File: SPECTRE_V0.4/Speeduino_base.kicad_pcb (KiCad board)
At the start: 2 copper layers, 100 x 93 mm, 161 parts, among them IC1 LM340?-MP, J1 Conn_01x04_Male, Q1 2N7002, Q10 BSP78, Q11 BSP78, Q12 BSP78, Q13 BSP78, Q2 CJ2302, Q3 CJ2302, Q4 CJ2302, Q5 BSP78, Q6 BSP78, Q7 CJ2302, Q8 CJ2302, Q9 CJ2302, U1 MAX9926UAEE+, U2 molex_48pin

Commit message: Cleaned up V0.4 Bug fixes in board V0.4 Changed readme to add more to be tested functions
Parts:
- added D22: D_Small, Diode_SMD:D_SOD-128, F.Cu at (85.3, 11.4)
- added D23: D_Small, Diode_SMD:D_SOD-128, F.Cu at (85.3, 15.5)
- added D24: D_Small, Diode_SMD:D_SOD-128, F.Cu at (92.7, 11.4)
- added D25: D_Small, Diode_SMD:D_SOD-128, F.Cu at (92.7, 15.5)
- added R73: 1k, Speeduino_base:R0603, F.Cu at (149.9, 15.9)
- added R74: 1k, Speeduino_base:R0603, F.Cu at (152.3, 15.9)
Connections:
- C15 pad 2: /PC6 -> /PC5
- D12 pad 3: /PC6 -> /PC5
- JP11 pad 2: Net-(D1-Pad3) -> Net-(JP11-Pad2)
- JP12 pad 2: Net-(D4-Pad3) -> Net-(JP12-Pad2)
- R27 pad 1: /PA6 -> /PA4
- R28 pad 2: Net-(R28-Pad2) -> 3.3V
- R33 pad 2: /PC6 -> /PC5

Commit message: Lots of changes, started new PCB with 8 inj channels.
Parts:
- removed F3, F4: PPTC 16V2A, Speeduino_base:1812L
- removed F5, F6, F7: PPTC 16V2A, Fuse:Fuse_1812_4532Metric
- removed IC1: LM340?-MP, Speeduino_base:SOT223
- removed JP15, JP5, JP6, JP7, JP8: SolderJumper_3_Bridged12, Jumper:SolderJumper-3_P1.3mm_Bridged12_Pad1.0x1.5mm
- removed U$1: A4988BREAKOUT, Speeduino_base:A4988BREAKOUT
- added A1: Pololu_Breakout_DRV8825, Module:Pololu_Breakout-16_15.2x20.3mm, F.Cu at (183.0, 65.8)
- added D26: 1N4007, Diode_SMD:D_SOD-128, B.Cu at (207.6, 43.8)
- added F2: PPTC 16V2A, Resistor_SMD:R_1812_4532Metric_Pad1.30x3.40mm_HandSolder, F.Cu at (176.7, 48.5)
- added Q14: BSP78, Speeduino_base:SOT223, F.Cu at (177.2, 89.9)
- added Q15: BSP78, Speeduino_base:SOT223, B.Cu at (191.0, 60.2)
- added Q16: BSP78, Speeduino_base:SOT223, B.Cu at (191.0, 42.6)
- added Q17: BSP78, Speeduino_base:SOT223, B.Cu at (191.0, 51.4)
- added Q18: BSP78, Speeduino_base:SOT223, B.Cu at (191.0, 33.8)
- added R75: 10k, Resistor_SMD:R_0603_1608Metric_Pad1.05x0.95mm_HandSolder, F.Cu at (145.7, 102.1)
- added R76: 10k, Resistor_SMD:R_0603_1608Metric_Pad1.05x0.95mm_HandSolder, F.Cu at (145.7, 106.7)
- added R77: 100, Speeduino_base:R0603, F.Cu at (164.6, 89.9)
- added R78: 10k, Speeduino_base:R0603, F.Cu at (168.3, 89.9)
- added R79: 10k, Speeduino_base:R0603, F.Cu at (170.7, 37.5)
- added R80: 10k, Speeduino_base:R0603, F.Cu at (174.5, 37.5)
- added R81: 10k, Speeduino_base:R0603, F.Cu at (168.8, 37.5)
- added R82: 10k, Speeduino_base:R0603, F.Cu at (172.6, 37.5)
- added U3: LM78M05_TO220, Package_TO_SOT_THT:TO-220-3_Vertical, F.Cu at (132.0, 37.8)
- D22, D23, D24, D25: value D_Small -> 1N4007
- F1: footprint Speeduino_base:1812L -> Resistor_SMD:R_1812_4532Metric_Pad1.30x3.40mm_HandSolder
- J1: footprint Connector_PinHeader_2.54mm:PinHeader_1x04_P2.54mm_Vertical -> Connector_PinHeader_2.00mm:PinHeader_1x04_P2.00mm_Vertical_SMD_Pin1Left
- R2: footprint Speeduino_base:R0603 -> Resistor_SMD:R_0603_1608Metric_Pad1.05x0.95mm_HandSolder
- R23: footprint Speeduino_base:R-7,5 -> Varistor:RV_Disc_D12mm_W3.9mm_P7.5mm
- moved D22 94.0 mm to (167.0, 58.0), turned to 90 degrees
- moved D25 93.2 mm to (182.8, 39.3), turned to 270 degrees
- moved D24 90.2 mm to (178.4, 39.4), turned to 270 degrees
- moved D23 88.4 mm to (162.8, 58.1), turned to 90 degrees
- moved C15 83.3 mm to (166.5, 22.1), turned to 180 degrees
- moved C12 81.4 mm to (169.1, 22.1), turned to 180 degrees
- moved R33 81.2 mm to (174.3, 22.1)
- moved R31 80.7 mm to (171.7, 22.1), turned to 180 degrees
- moved R30 80.6 mm to (176.9, 22.1), turned to 0 degrees
- moved D12 79.9 mm to (162.5, 23.7)
- moved R54 66.2 mm to (203.8, 99.4), turned to 180 degrees
- moved D9 64.0 mm to (201.9, 102.4), turned to 270 degrees
- moved R26 63.6 mm to (201.9, 99.4), turned to 180 degrees
- moved D17 62.1 mm to (203.8, 102.4), turned to 270 degrees
- moved R74 60.3 mm to (121.2, 67.6), turned to 180 degrees
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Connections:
- net /PA0 renamed PA0
- net /PA11 renamed Net-(JP3-Pad32)
- net /PA12 renamed Net-(JP3-Pad31)
- net /PA15 renamed Net-(JP3-Pad30)
- net /PA5 renamed PA5
- net /PA6 renamed Net-(JP1-Pad29)
- net /PA7 renamed Net-(JP1-Pad30)
- net /PA8 renamed PA8
- net /PB0 renamed Net-(JP1-Pad33)
- net /PB11 renamed PB11
- net /PB12 renamed PB12
- net /PB13 renamed PB13
- net /PB14 renamed PB14
- net /PB15 renamed PB15
- net /PB3 renamed PB3
- net /PB5 renamed PB5
- net /PB6 renamed PB6
- net /PB7 renamed PB7
- net /PB8 renamed PB8
- net /PB9 renamed PB9
- net /PC0 renamed PC0
- net /PC10 renamed Net-(JP3-Pad29)
- net /PC11 renamed Net-(JP3-Pad28)
- net /PC12 renamed Net-(JP3-Pad27)
- net /PC2 renamed PC2
- net /PC4 renamed PC4
- net /PC5 renamed PC5
- net /PC6 renamed PC6
- net /PC9 renamed Net-(JP3-Pad36)
- net /PD0 renamed PD0
- net /PD1 renamed PD1
- net /PD11 renamed PD11
- net /PD2 renamed Net-(JP3-Pad24)
- net /PD4 renamed PD4
- net /PD5 renamed PD5
- net /PD6 renamed PD6
- net /PD7 renamed PD7
- net /PD8 renamed PD8
- net /PD9 renamed PD9
- net /PE10 renamed PE10
- net /PE15 renamed PE15
- net /PE4 renamed PE4
- net /PE6 renamed PE6
- net /PE8 renamed PE8
- net /PE9 renamed PE9
- net /VREF+ renamed Net-(JP1-Pad22)
- net /VREF- renamed Net-(JP1-Pad21)
- C13 pad 2: Net-(C13-Pad2) -> PC3
- C23 pad 2: Net-(C23-Pad2) -> PA1
- C24 pad 2: Net-(C24-Pad2) -> PC1
- D11 pad 3: /PC3 -> PC3
- D16 pad 3: /PC1 -> PC1
- D24 pad 2: IDLE2-OUT -> IDLE1-OUT
- D25 pad 2: IDLE1-OUT -> IDLE2-OUT
- JP1 pad 11: /PE2 -> PE2
- JP1 pad 12: /PE3 -> PE3
- JP1 pad 14: /PE5 -> PE5
- JP1 pad 18: /PC1 -> PC1
- JP1 pad 20: /PC3 -> PC3
- JP1 pad 27: /PA4 -> PA4
- JP1 pad 35: /PE7 -> PE7
- JP1 pad 39: /PE11 -> PE11
- JP1 pad 40: /PE12 -> PE12
- JP1 pad 41: /PE13 -> PE13
- JP1 pad 42: /PE14 -> PE14
- JP1 pad 44: /PB10 -> PB10
- JP10 pad 3: STEP_2A_OUT -> STEP_1A_OUT
- JP3 pad 38: /PC7 -> PC7
- JP3 pad 45: /PD10 -> PD10
- JP9 pad 3: STEP_1A_OUT -> STEP_2A_OUT
- Q10 pad 2: IDLE1-OUT -> IDLE2-OUT
- Q10 pad 4: IDLE1-OUT -> IDLE2-OUT
- Q11 pad 2: IDLE2-OUT -> IDLE1-OUT
- Q11 pad 4: IDLE2-OUT -> IDLE1-OUT
- Q3 pad 2: GND -> PWR_GND
- R14 pad 2: Net-(R14-Pad2) -> Net-(C6-Pad1)
- R26 pad 2: VBAT_F1 -> VBAT
- R27 pad 1: /PA4 -> PE3
- R32 pad 2: /PC3 -> PC3
- R39 pad 2: /PC1 -> PC1
- R44 pad 2: GND -> PWR_GND
- R54 pad 2: VBAT_F1 -> VBAT
- R6 pad 2: Net-(R6-Pad2) -> Net-(C5-Pad2)
- R65 pad 2: /PB10 -> PD10
- U1 pad 10: Net-(R14-Pad2) -> Net-(C6-Pad1)
- U1 pad 16: Net-(R6-Pad2) -> Net-(C5-Pad2)
- U2 pad 1: VBAT -> PWR_GND
- U2 pad 10: PWR_GND -> BARO
- U2 pad 11: Net-(JP8-Pad2) -> STEP_2B_OUT
- U2 pad 12: Net-(JP9-Pad2) -> STEP_1B_OUT
- U2 pad 13: STEP_2B_OUT -> IGN1-OUT
- U2 pad 15: FUEL_PUMP -> FAN
- U2 pad 16: INJ4-OUT -> IGN4-OUT
- U2 pad 17: Net-(JP10-Pad2) -> FUEL_PUMP
- U2 pad 18: VR2+ -> Net-(U2-Pad18)
- U2 pad 19: FAN -> VR2+
- U2 pad 2: VBAT -> PWR_GND
- U2 pad 20: INJ3-OUT -> Net-(JP9-Pad2)
- U2 pad 21: VR1- -> CLT_2
- U2 pad 23: TPS -> VR1-
- U2 pad 24: IGN1-OUT -> INJ4-OUT
- U2 pad 25: Net-(JP5-Pad2) -> GND
- U2 pad 28: INJ2-OUT -> INJ3-OUT
- U2 pad 29: Net-(JP6-Pad2) -> GND
- U2 pad 3: PWR_GND -> VBAT
- U2 pad 33: Net-(JP7-Pad2) -> GND
- U2 pad 34: 3.3V -> TPS
- U2 pad 37: V_O2 -> Net-(U2-Pad37)
- U2 pad 38: V_IGN -> FLEX_FUEL_IN
- U2 pad 4: PWR_GND -> VBAT
- U2 pad 41: V_IGN -> O2_2
- U2 pad 42: V_IGN -> IAT_2
- U2 pad 43: 5V -> Net-(U2-Pad43)
- U2 pad 44: IGN4-OUT -> INJ2-OUT
- U2 pad 45: V_IGN -> 5V
- U2 pad 46: PWR_GND -> 3.3V
- U2 pad 47: Net-(JP15-Pad2) -> BOOST-OUT
- U2 pad 5: V_INJ34 -> INJ8-OUT
- U2 pad 6: V_INJ34 -> INJ7-OUT
- U2 pad 7: V_INJ12 -> INJ5-OUT
- U2 pad 8: V_INJ12 -> INJ6-OUT
- U2 pad 9: PWR_GND -> Net-(JP10-Pad2)
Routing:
- net GND: track 625.1 -> 299.6 mm, vias 32 -> 4
- net 3.3V: track 559.6 -> 426.3 mm, vias 21 -> 8
- net PD13: track 143.4 -> 32.2 mm, vias 2 -> 0
- net VR2+: track 187.0 -> 77.0 mm, vias 2 -> 3
- net /PE5: track 105.6 -> 0.00 mm, vias 1 -> 0
- net Net-(Q4-Pad1): track 100.9 -> 5.86 mm, vias 4 -> 0
- net VR1-: track 176.3 -> 84.3 mm, vias 0 -> 3
- net VR2-: track 161.8 -> 74.1 mm, vias 0 -> 2
- net VR1+: track 195.1 -> 110.7 mm, vias 0 -> 3
- net BOOST-OUT: track 0.00 -> 82.6 mm, vias 0 -> 1
- net /PB10: track 81.6 -> 0.00 mm, vias 1 -> 0
- net Net-(JP15-Pad2): track 74.4 -> 0.00 mm, vias 1 -> 0
- net FLEX_FUEL_IN: track 6.26 -> 80.5 mm, vias 0 -> 1
- net PC13: track 69.6 -> 0.00 mm, vias 2 -> 0
- net VBAT_F1: track 100.7 -> 31.9 mm, vias 4 -> 0
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- removed copper zone on F.Cu, net 3.3V
- removed copper zone on F.Cu, net 5V
- removed copper zone on F.Cu, net IDLE1-OUT
- removed copper zone on F.Cu, net IDLE2-OUT
- removed copper zone on B.Cu, net INJ1-OUT
- removed copper zone on B.Cu, net INJ2-OUT
- removed copper zone on B.Cu, net INJ3-OUT
- removed copper zone on B.Cu, net INJ4-OUT
- removed copper zone on B.Cu, net PWR_GND
- removed copper zone on F.Cu, net VBAT
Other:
- board text added: "SPEEDUINO STM32F4 TESTBOARD NR4"
- board text removed: "SPEEDUINO STM32F4 TESTBOARD NR3"

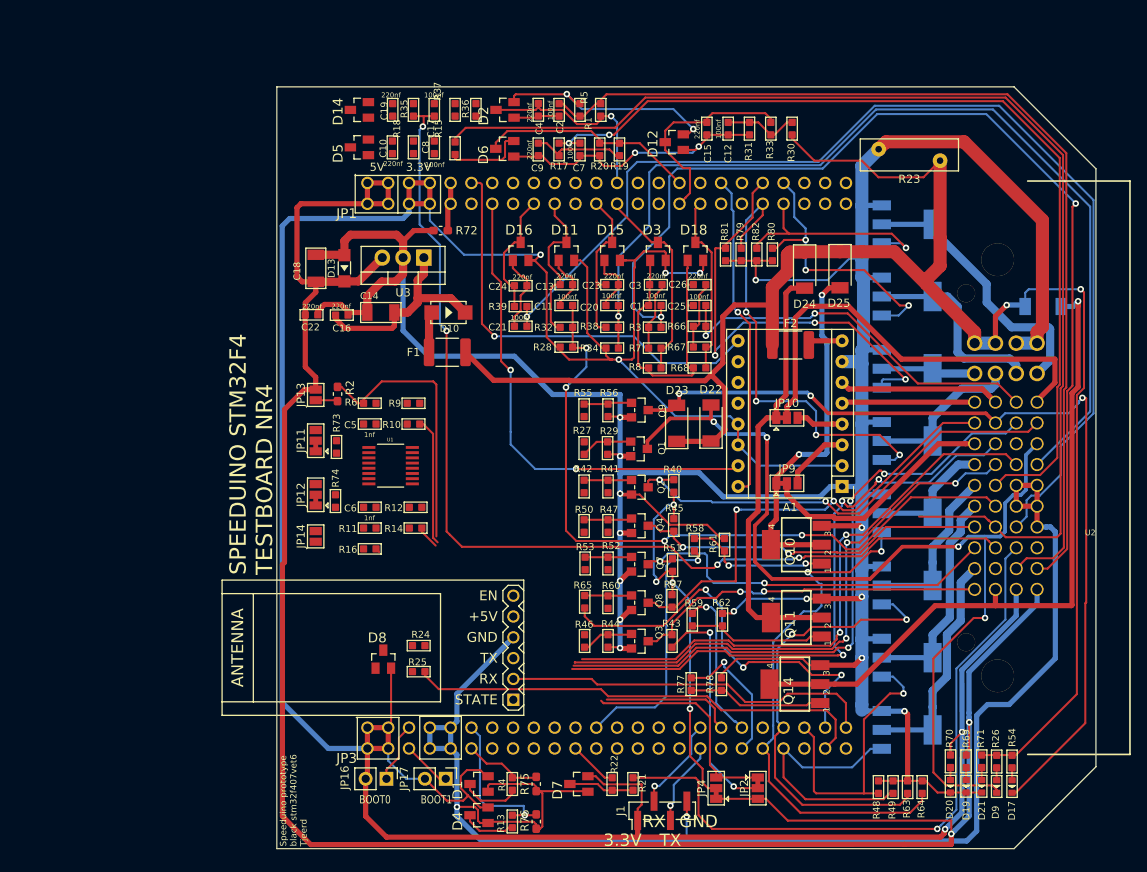
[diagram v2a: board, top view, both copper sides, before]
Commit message: All tracks routed: TODO: Copper GND, Copper Cooling transistors, Check to220 5v direction
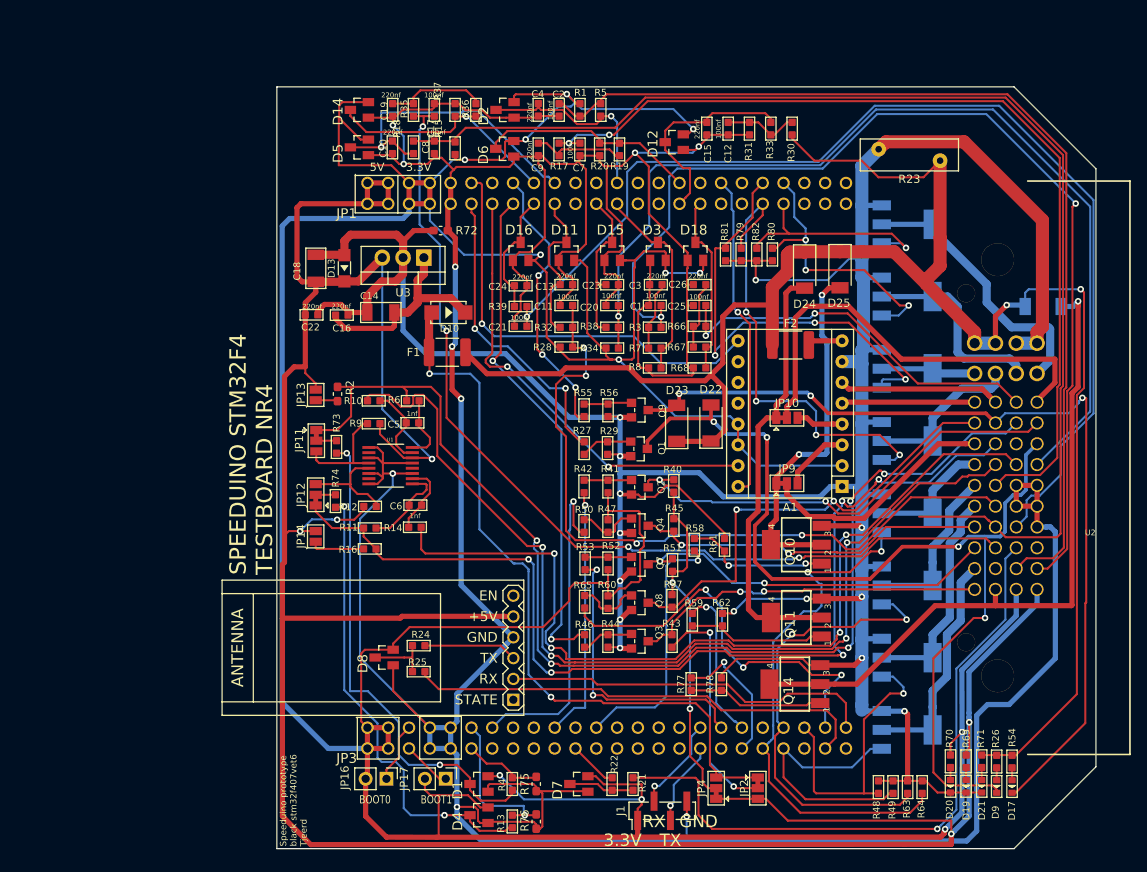
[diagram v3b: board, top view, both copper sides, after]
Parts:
- moved R10 5.62 mm to (125.8, 55.3), turned to 90 degrees
- moved C6 5.57 mm to (130.9, 68.1)
- moved R12 5.56 mm to (125.4, 68.2)
- moved R9 5.45 mm to (125.8, 58.1), turned to 90 degrees
- moved R6 5.27 mm to (130.6, 55.3)
- moved C5 5.21 mm to (130.6, 58.0), turned to 90 degrees
- moved D8 0.23 mm to (127.1, 86.7), turned to 90 degrees
- moved R14 0.13 mm to (130.9, 70.8)
- moved JP11 0.08 mm to (118.8, 60.2), turned to 270 degrees
- turned R11 to 90 degrees
- turned R47 to 180 degrees
- turned R60 to 180 degrees
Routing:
- net GND: track 299.6 -> 525.8 mm, vias 4 -> 10
- net 3.3V: track 426.3 -> 540.0 mm, vias 8 -> 12
- net 5V: track 262.3 -> 342.1 mm, vias 2 -> 5
- net PC13: track 0.00 -> 62.5 mm, vias 0 -> 2
- net VBAT_F1: track 31.9 -> 90.0 mm, vias 0 -> 2
- net Net-(D1-Pad3): track 7.23 -> 59.8 mm, vias 0 -> 2
- net Net-(D4-Pad3): track 6.55 -> 57.0 mm, vias 0 -> 2
- net VR2+: track 77.0 -> 124.7 mm, vias 3 -> 5
- net PB9: track 0.00 -> 40.0 mm, vias 0 -> 1
- net PC2: track 0.00 -> 37.9 mm, vias 0 -> 1
- net PE3: track 0.00 -> 37.3 mm, vias 0 -> 2
- net VR1-: track 84.3 -> 120.3 mm, vias 3 -> 4
- net PE6: track 0.00 -> 33.9 mm, vias 0 -> 3
- net VR2-: track 74.1 -> 107.4 mm, vias 2 -> 4
- net VR1+: track 110.7 -> 142.6 mm, vias 3 -> 5
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
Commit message: Added copper planes
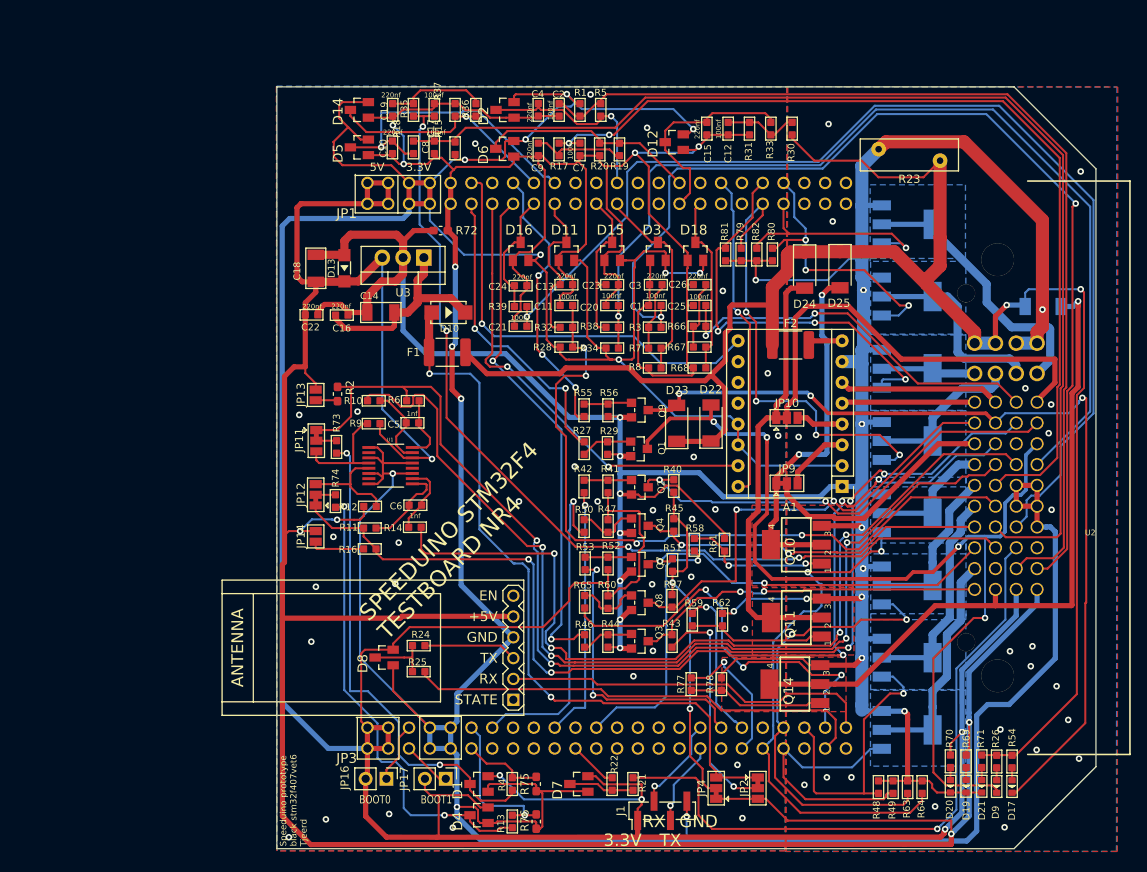
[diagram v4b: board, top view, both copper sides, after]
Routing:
- net IAT: track 149.6 -> 139.8 mm
- net PE11: track 56.1 -> 51.0 mm
- net GND: track 525.8 -> 527.4 mm, vias 10 -> 41
- net PE0: track 9.70 -> 10.4 mm
- net PD13: track 32.2 -> 32.8 mm
- net PWR_GND: track 390.3 -> 390.6 mm, vias 14 -> 38
- net (no net): vias 0 -> 1
- added copper zone on F.Cu, net BOOST-OUT
- added copper zone on B.Cu, net GND
- added copper zone on F.Cu, net GND
- added copper zone on F.Cu, net IDLE1-OUT
- added copper zone on F.Cu, net IDLE2-OUT
- added copper zone on B.Cu, net INJ1-OUT
- added copper zone on B.Cu, net INJ2-OUT
- added copper zone on B.Cu, net INJ3-OUT
- added copper zone on B.Cu, net INJ4-OUT
- added copper zone on B.Cu, net INJ5-OUT
- added copper zone on B.Cu, net INJ6-OUT
- added copper zone on B.Cu, net INJ7-OUT
- added copper zone on B.Cu, net INJ8-OUT
- added copper zone on B.Cu, net PWR_GND
- added copper zone on F.Cu, net PWR_GND
